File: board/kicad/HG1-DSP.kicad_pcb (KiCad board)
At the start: 12 copper layers, 150 x 150 mm, 29 parts, among them J2 Samtec LSHM-150 (mate ANT), J3 Samtec LSHM-150 (mate ANT), J4 Samtec LSHM-120 (mate ANT), J5 FFC to PWR/IO: GbE MDI, RS-48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, J6 Micro-Fit 4p: +12V_DSP in, U1 XCVE2302-1LSESFVA784 Versal A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, U10 nRF7002 Wi-Fi 6 2.4/5 GHz com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, U11 ISM330DHCX 6-axis IMU, U12 LIS2MDL magnetometer, U2 LPDDR4 32Gb x32 (MT53E1G32D2), U20 TPS546D24A 40 A PoL VCCINT 0.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, U21 TPS546D24A PoL VCC_AIE 0.8 V, U22 LT8640S 1V1/1V8/3V3 bucks, U3 LPDDR4 32Gb x32 (MT53E1G32D2), U4 eMMC 64 GB pSLC, U5 QSPI NOR 512 Mb (boot), U6 DP83867IR GbE PHY + IEEE1588 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, U7 STM32G474 housekeeping / powe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, U8 u-blox NEO-F10T GNSS timing (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, U9 nRF52840 BT5 LR Remote-ID rx

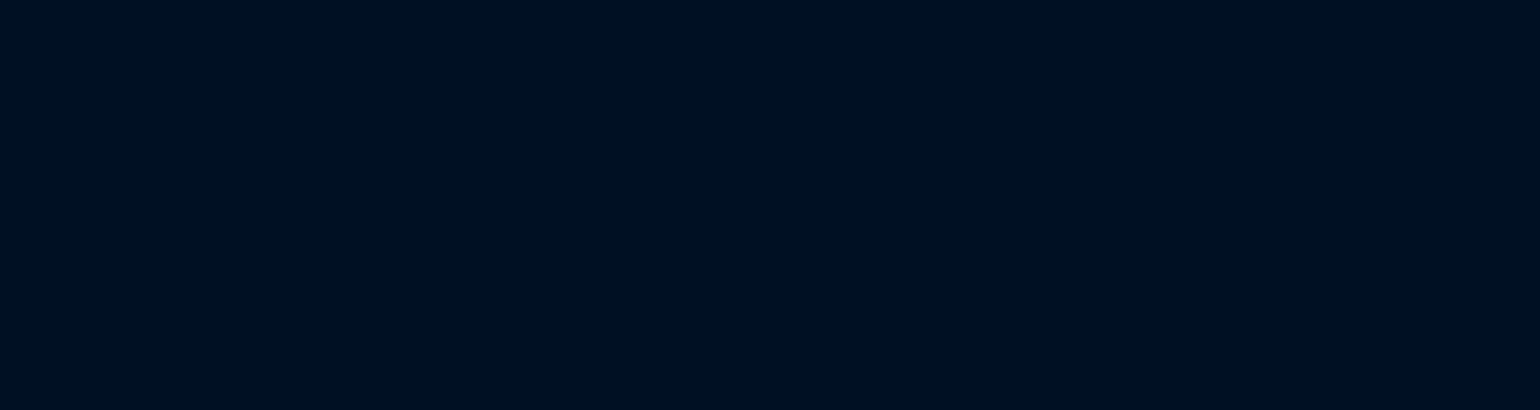
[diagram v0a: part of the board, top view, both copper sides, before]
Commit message: Schematics, full-wave EM element optimisation, physical stack-ups
Schematics
- KiCad schematics for HG1-ANT/DSP/PWR generated by board/schematic/
  (33-symbol HG1 library, pins taken from the routed layout): ERC 0/0,
  schematic<->PCB parity clean; scripted "Update PCB from Schematic"
  links footprints, nets and values and stages unplaced parts.
- STM32G474 pin map corrected to the real LQFP-64 pin-out.

Full-wave EM of the radiating element (antenna/em, docs/06)
- EMerge FEM models: isolated element and infinite-array unit cell with
  a scan-matched Floquet port; local PARDISO and Modal (CPU, cuDSS GPU).
- Found and fixed: low slot/superstrate resonance of the analytic cut,
  60 deg azimuth scan blindness (element via-fence cavity), far-field
  dB scaling and E/H cut labelling.
- Differential evolution on Modal (792 solves, worst of 0/45/60 deg):
  driven 3.21 mm, parasitic 4.48 mm, slot 3.02 mm + 2.14 mm arms,
  stub 1.50 mm, 1.016 mm parasitic spacer. Active |S11| < -10 dB over
  0.52-0.70 GHz around 16 GHz at every scan to 60 az / 40 el.

Board / mechanical
- New element copper and 1,051 blind L1-L5 element-fence vias on ANT.
- Full physical stack-ups (hg1_params.STACKS) written into each
  .kicad_pcb; ANT is 2.716 mm (old 2.1 mm could not hold 10 layers).
- Enclosure, mass (1,059 g), KiCad and Blender renders regenerated.
  DRC 0 errors on all boards, parity clean.

Co-Authored-By: Claude Opus 5.5 <noreply@anthropic.com>
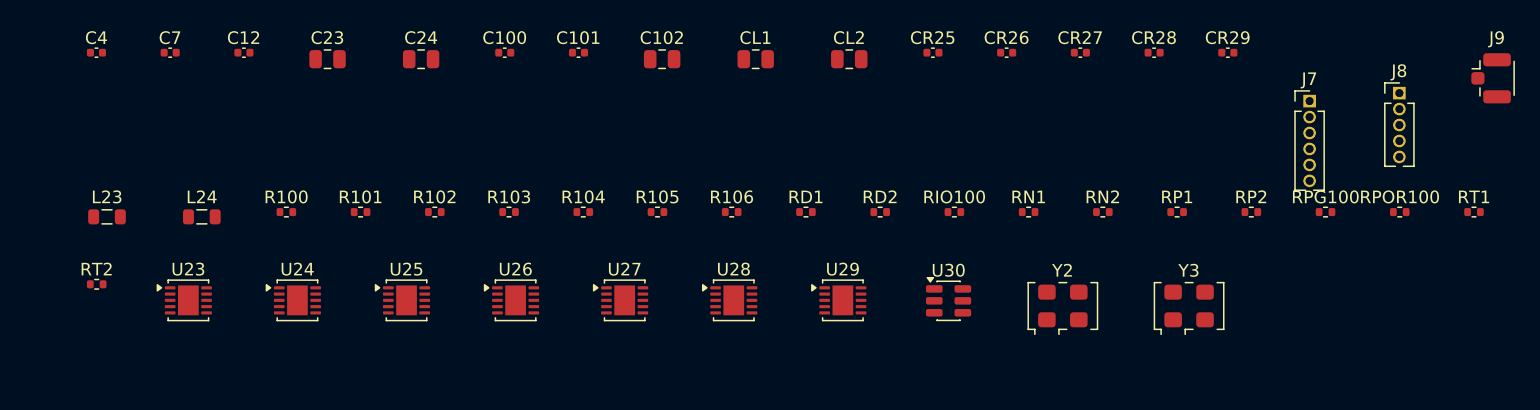
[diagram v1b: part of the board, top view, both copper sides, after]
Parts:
- added C100: 100n, Capacitor_SMD:C_0402_1005Metric, F.Cu at (275.4, 37.5)
- added C101: 1u, Capacitor_SMD:C_0402_1005Metric, F.Cu at (281.3, 37.5)
- added C102: 47u, Capacitor_SMD:C_0805_2012Metric, F.Cu at (288.0, 38.0)
- added C12: 220n, Capacitor_SMD:C_0402_1005Metric, F.Cu at (254.7, 37.5)
- added C23: 22u, Capacitor_SMD:C_0805_2012Metric, F.Cu at (261.3, 38.0)
- added C24: 22u, Capacitor_SMD:C_0805_2012Metric, F.Cu at (268.8, 38.0)
- added C4: 1u, Capacitor_SMD:C_0402_1005Metric, F.Cu at (242.9, 37.5)
- added C7: 100n, Capacitor_SMD:C_0402_1005Metric, F.Cu at (248.8, 37.5)
- added CL1: 470u polymer, Capacitor_SMD:C_0805_2012Metric, F.Cu at (295.4, 38.0)
- added CL2: 470u polymer, Capacitor_SMD:C_0805_2012Metric, F.Cu at (302.9, 38.0)
- added CR25: 1u, Capacitor_SMD:C_0402_1005Metric, F.Cu at (309.5, 37.5)
- added CR26: 1u, Capacitor_SMD:C_0402_1005Metric, F.Cu at (315.4, 37.5)
- added CR27: 1u, Capacitor_SMD:C_0402_1005Metric, F.Cu at (321.3, 37.5)
- added CR28: 1u, Capacitor_SMD:C_0402_1005Metric, F.Cu at (327.1, 37.5)
- added CR29: 1u, Capacitor_SMD:C_0402_1005Metric, F.Cu at (333.0, 37.5)
- added J7: JTAG, Connector_PinHeader_1.27mm:PinHeader_1x06_P1.27mm_Vertical, F.Cu at (339.5, 41.3)
- added J8: SWD (Tag-Connect TC2030), Connector_PinHeader_1.27mm:PinHeader_1x05_P1.27mm_Vertical, F.Cu at (346.7, 40.7)
- added J9: U.FL OTA-cal port, Connector_Coaxial:U.FL_Hirose_U.FL-R-SMT-1_Vertical, F.Cu at (354.4, 39.5)
- added L23: 2.2u, Inductor_SMD:L_0805_2012Metric, F.Cu at (243.8, 50.6)
- added L24: 2.2u, Inductor_SMD:L_0805_2012Metric, F.Cu at (251.3, 50.6)
- added R100: 1M, Resistor_SMD:R_0402_1005Metric, F.Cu at (258.1, 50.2)
- added R101: 316k, Resistor_SMD:R_0402_1005Metric, F.Cu at (264.0, 50.2)
- added R102: 18.2k, Resistor_SMD:R_0402_1005Metric, F.Cu at (269.9, 50.2)
- added R103: 100k, Resistor_SMD:R_0402_1005Metric, F.Cu at (275.8, 50.2)
- added R104: 49.9k, Resistor_SMD:R_0402_1005Metric, F.Cu at (281.7, 50.2)
- added R105: 100k, Resistor_SMD:R_0402_1005Metric, F.Cu at (287.6, 50.2)
- added R106: 49.9k, Resistor_SMD:R_0402_1005Metric, F.Cu at (293.5, 50.2)
- added RD1: 10k, Resistor_SMD:R_0402_1005Metric, F.Cu at (299.4, 50.2)
- added RD2: 10k, Resistor_SMD:R_0402_1005Metric, F.Cu at (305.3, 50.2)
- added RIO100: 0R (3.3 V to PWR/IO board), Resistor_SMD:R_0402_1005Metric, F.Cu at (311.2, 50.2)
- added RN1: 20k 0.1%, Resistor_SMD:R_0402_1005Metric, F.Cu at (317.2, 50.2)
- added RN2: 40.2k 0.1%, Resistor_SMD:R_0402_1005Metric, F.Cu at (323.1, 50.2)
- added RP1: 10k 0.1%, Resistor_SMD:R_0402_1005Metric, F.Cu at (329.0, 50.2)
- added RP2: 10k 0.1%, Resistor_SMD:R_0402_1005Metric, F.Cu at (334.9, 50.2)
- added RPG100: 10k, Resistor_SMD:R_0402_1005Metric, F.Cu at (340.8, 50.2)
- added RPOR100: 4.7k, Resistor_SMD:R_0402_1005Metric, F.Cu at (346.7, 50.2)
- added RT1: 10k B3435, Resistor_SMD:R_0402_1005Metric, F.Cu at (352.6, 50.2)
- added RT2: 10k B3435, Resistor_SMD:R_0402_1005Metric, F.Cu at (243.0, 55.9)
- added U23: TPS62913 1.8 V, Package_DFN_QFN:DFN-10-1EP_3x3mm_P0.5mm_EP1.65x2.38mm, F.Cu at (250.3, 57.2)
- added U24: TPS62913 1.1 V, Package_DFN_QFN:DFN-10-1EP_3x3mm_P0.5mm_EP1.65x2.38mm, F.Cu at (258.9, 57.2)
- added U25: ADP7159 1.5 V LDO, Package_DFN_QFN:DFN-10-1EP_3x3mm_P0.5mm_EP1.65x2.38mm, F.Cu at (267.6, 57.2)
- added U26: ADP7159 0.88 V LDO, Package_DFN_QFN:DFN-10-1EP_3x3mm_P0.5mm_EP1.65x2.38mm, F.Cu at (276.3, 57.2)
- added U27: ADP7159 1.2 V LDO, Package_DFN_QFN:DFN-10-1EP_3x3mm_P0.5mm_EP1.65x2.38mm, F.Cu at (285.0, 57.2)
- added U28: ADP7159 2.5 V LDO, Package_DFN_QFN:DFN-10-1EP_3x3mm_P0.5mm_EP1.65x2.38mm, F.Cu at (293.7, 57.2)
- added U29: ADP7159 1.0 V LDO, Package_DFN_QFN:DFN-10-1EP_3x3mm_P0.5mm_EP1.65x2.38mm, F.Cu at (302.4, 57.2)
- added U30: TPS3700 -5 V window, Package_TO_SOT_SMD:SOT-23-6, F.Cu at (310.8, 57.2)
- added Y2: 33.333 MHz XO (PS_REFCLK), Oscillator:Oscillator_SMD_EuroQuartz_XO53-4Pin_5.0x3.2mm, F.Cu at (319.9, 57.7)
- added Y3: 25 MHz XO, Oscillator:Oscillator_SMD_EuroQuartz_XO53-4Pin_5.0x3.2mm, F.Cu at (329.9, 57.7)
- H1, H2, H3, H4, H5, H6: footprint MountingHole_2.7mm_M2.5_Pad_Via -> MountingHole:MountingHole_2.7mm_M2.5_Pad_Via
- J2, J3: value Samtec LSHM-150 (mate ANT) -> LSHM-150 (mate ANT); footprint Samtec_LSHM-150-xx.x-x-DV-N_2x50_P0.50mm_Vertical -> Connector_Samtec:Samtec_LSHM-150-xx.x-x-DV-N_2x50_P0.50mm_Vertical
- J4: value Samtec LSHM-120 (mate ANT) -> LSHM-120 (mate ANT); footprint Samtec_LSHM-120-xx.x-x-DV-N_2x20_P0.50mm_Vertical -> Connector_Samtec:Samtec_LSHM-120-xx.x-x-DV-N_2x20_P0.50mm_Vertical
- J5: value FFC to PWR/IO: GbE MDI, RS-485, 1PPS, discretes -> FFC to PWR/IO; footprint Hirose_FH12-30S-0.5SH_1x30-1MP_P0.50mm_Horizontal -> Connector_FFC-FPC:Hirose_FH12-30S-0.5SH_1x30-1MP_P0.50mm_Horizontal
- J6: value Micro-Fit 4p: +12V_DSP in -> Micro-Fit +12V in; footprint Molex_Micro-Fit_3.0_43650-0400_1x04_P3.00mm_Horizontal -> Connector_Molex:Molex_Micro-Fit_3.0_43650-0400_1x04_P3.00mm_Horizontal
- L1, L2: value XAL6030 0.22 uH -> XAL6030 0.22u; footprint L_Coilcraft_XAL6030-XXX -> Inductor_SMD:L_Coilcraft_XAL6030-XXX
- L3: value XAL6030 1.0 uH -> XAL6030 1.0u; footprint L_Coilcraft_XAL6030-XXX -> Inductor_SMD:L_Coilcraft_XAL6030-XXX
- U1: value XCVE2302-1LSESFVA784 Versal AI Edge (AIE-ML 3D beamforming) -> XCVE2302-1LSESFVA784; footprint Microchip_FCVG784_BGA-784_23x23mm_Layout28x28_P0.8mm -> Package_BGA:Microchip_FCVG784_BGA-784_23x23mm_Layout28x28_P0.8mm
- U10: value nRF7002 Wi-Fi 6 2.4/5 GHz companion: Wi-Fi Beacon/NAN Remote-ID rx (fed from ANT RID patch) -> nRF7002; footprint QFN-40-1EP_6x6mm_P0.5mm_EP4.6x4.6mm -> Package_DFN_QFN:QFN-40-1EP_6x6mm_P0.5mm_EP4.6x4.6mm
- U11: value ISM330DHCX 6-axis IMU -> ISM330DHCX; footprint Bosch_LGA-14_3x2.5mm_P0.5mm -> Package_LGA:Bosch_LGA-14_3x2.5mm_P0.5mm
- U12: value LIS2MDL magnetometer -> LIS2MDL; footprint LGA-12_2x2mm_P0.5mm -> Package_LGA:LGA-12_2x2mm_P0.5mm
- U2, U3: value LPDDR4 32Gb x32 (MT53E1G32D2) -> MT53E1G32D2 LPDDR4; footprint BGA-200_10x14.5mm_Layout12x22_P0.8x0.65mm -> Package_BGA:BGA-200_10x14.5mm_Layout12x22_P0.8x0.65mm
- U20: value TPS546D24A 40 A PoL VCCINT 0.8 V -> TPS546D24A 0.8 V; footprint QFN-40-1EP_6x6mm_P0.5mm_EP4.6x4.6mm_ThermalVias -> Package_DFN_QFN:QFN-40-1EP_6x6mm_P0.5mm_EP4.6x4.6mm_ThermalVias
- U21: value TPS546D24A PoL VCC_AIE 0.8 V -> TPS546D24A 0.8 V; footprint QFN-40-1EP_6x6mm_P0.5mm_EP4.6x4.6mm_ThermalVias -> Package_DFN_QFN:QFN-40-1EP_6x6mm_P0.5mm_EP4.6x4.6mm_ThermalVias
- U22: value LT8640S 1V1/1V8/3V3 bucks -> LT8640S 3.3 V; footprint QFN-24-1EP_4x4mm_P0.5mm_EP2.6x2.6mm -> Package_DFN_QFN:QFN-24-1EP_4x4mm_P0.5mm_EP2.6x2.6mm
- U4: footprint LFBGA-153_11.5x13mm_Layout14x14_P0.5mm -> Package_BGA:LFBGA-153_11.5x13mm_Layout14x14_P0.5mm
- U5: value QSPI NOR 512 Mb (boot) -> MT25QU512 QSPI; footprint WSON-8-1EP_8x6mm_P1.27mm_EP3.4x4.3mm -> Package_SON:WSON-8-1EP_8x6mm_P1.27mm_EP3.4x4.3mm
- U6: value DP83867IR GbE PHY + IEEE1588 SFD -> DP83867IRRGZ; footprint QFN-48-1EP_7x7mm_P0.5mm_EP5.6x5.6mm -> Package_DFN_QFN:QFN-48-1EP_7x7mm_P0.5mm_EP5.6x5.6mm
- U7: value STM32G474 housekeeping / power-seq / BIT -> STM32G474RET6; footprint LQFP-64_10x10mm_P0.5mm -> Package_QFP:LQFP-64_10x10mm_P0.5mm
- U8: value u-blox NEO-F10T GNSS timing (L1/L5) -> NEO-F10T (NEO footprint); footprint ublox_NEO -> RF_GPS:ublox_NEO
- U9: value nRF52840 BT5 LR Remote-ID rx -> MDBT50Q nRF52840; footprint Raytac_MDBT50Q -> RF_Module:Raytac_MDBT50Q
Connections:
- J2 pad 1: (no net) -> GND
- J2 pad 10: (no net) -> GND
- J2 pad 100: (no net) -> JESD1_L0
- J2 pad 11: (no net) -> GND
- J2 pad 12: (no net) -> GND
- J2 pad 13: (no net) -> GND
- J2 pad 14: (no net) -> GND
- J2 pad 15: (no net) -> GND
- J2 pad 16: (no net) -> GND
- J2 pad 17: (no net) -> GND
- J2 pad 18: (no net) -> GND
- J2 pad 19: (no net) -> GND
- J2 pad 2: (no net) -> JESD3_L3
- J2 pad 20: (no net) -> JESD2_L3
- J2 pad 21: (no net) -> GND
- J2 pad 22: (no net) -> GND
- J2 pad 23: (no net) -> GND
- J2 pad 24: (no net) -> JESD2_L2
- J2 pad 25: (no net) -> GND
- J2 pad 26: (no net) -> JESD2_L1
- J2 pad 27: (no net) -> GND
- J2 pad 28: (no net) -> GND
- J2 pad 29: (no net) -> GND
- J2 pad 3: (no net) -> CAL_PROBE
- J2 pad 30: (no net) -> JESD2_L0
- J2 pad 31: (no net) -> GND
- J2 pad 32: (no net) -> GND
- J2 pad 33: (no net) -> GND
- J2 pad 34: (no net) -> GND
- J2 pad 35: (no net) -> GND
- J2 pad 36: (no net) -> GND
- J2 pad 37: (no net) -> GND
- J2 pad 38: (no net) -> GND
- J2 pad 39: (no net) -> GND
- J2 pad 4: (no net) -> JESD3_L2
- J2 pad 40: (no net) -> GND
- J2 pad 41: (no net) -> GND
- J2 pad 42: (no net) -> GND
- J2 pad 43: (no net) -> GND
- J2 pad 44: (no net) -> GND
- J2 pad 45: (no net) -> GND
- J2 pad 46: (no net) -> GND
- J2 pad 47: (no net) -> GND
- J2 pad 48: (no net) -> GND
- J2 pad 49: (no net) -> GND
- J2 pad 5: (no net) -> CAL_PROBE
- J2 pad 50: (no net) -> GND
- J2 pad 51: (no net) -> GND
- J2 pad 52: (no net) -> GND
- J2 pad 53: (no net) -> GND
- J2 pad 54: (no net) -> GND
- J2 pad 55: (no net) -> GND
- J2 pad 56: (no net) -> GND
- J2 pad 57: (no net) -> GND
- J2 pad 58: (no net) -> GND
- J2 pad 59: (no net) -> GND
- J2 pad 6: (no net) -> JESD3_L1
- J2 pad 60: (no net) -> GND
- J2 pad 61: (no net) -> GND
- J2 pad 62: (no net) -> GND
- J2 pad 63: (no net) -> GND
- J2 pad 64: (no net) -> GND
- J2 pad 65: (no net) -> GND
- J2 pad 66: (no net) -> GND
- J2 pad 67: (no net) -> GND
- J2 pad 68: (no net) -> GND
- J2 pad 69: (no net) -> GND
- J2 pad 7: (no net) -> CAL_PROBE
- J2 pad 70: (no net) -> GND
- J2 pad 71: (no net) -> GND
- J2 pad 72: (no net) -> GND
- J2 pad 73: (no net) -> GND
- J2 pad 74: (no net) -> GND
- J2 pad 75: (no net) -> GND
- J2 pad 76: (no net) -> GND
- J2 pad 77: (no net) -> GND
- J2 pad 78: (no net) -> GND
- J2 pad 79: (no net) -> GND
- J2 pad 8: (no net) -> JESD3_L0
- J2 pad 80: (no net) -> GND
- J2 pad 81: (no net) -> GND
- J2 pad 82: (no net) -> GND
- J2 pad 83: (no net) -> GND
- J2 pad 84: (no net) -> GND
- J2 pad 85: (no net) -> GND
- J2 pad 86: (no net) -> GND
- J2 pad 87: (no net) -> GND
- J2 pad 88: (no net) -> GND
- J2 pad 89: (no net) -> GND
- J2 pad 9: (no net) -> CAL_PROBE
- J2 pad 90: (no net) -> GND
- J2 pad 91: (no net) -> GND
- J2 pad 92: (no net) -> JESD1_L3
- J2 pad 93: (no net) -> GND
- J2 pad 94: (no net) -> GND
- J2 pad 95: (no net) -> GND
- J2 pad 96: (no net) -> JESD1_L2
- J2 pad 97: (no net) -> GND
- J2 pad 98: (no net) -> JESD1_L1
- J2 pad 99: (no net) -> GND
- J3 pad 1: (no net) -> GND
- J3 pad 10: (no net) -> JESD6_L1
- J3 pad 100: (no net) -> JESD4_L0
- J3 pad 11: (no net) -> ID_PA2
- J3 pad 12: (no net) -> GND
- J3 pad 13: (no net) -> GND
- J3 pad 14: (no net) -> JESD6_L0
- J3 pad 15: (no net) -> ID_PA3
- J3 pad 16: (no net) -> GND
- J3 pad 17: (no net) -> ID_PA4
- J3 pad 18: (no net) -> GND
- J3 pad 19: (no net) -> ID_PA5
- J3 pad 2: (no net) -> GND
- J3 pad 20: (no net) -> GND
- J3 pad 21: (no net) -> ID_PA6
- J3 pad 22: (no net) -> GND
- J3 pad 23: (no net) -> ID_PA1
- J3 pad 24: (no net) -> GND
- J3 pad 25: (no net) -> ID_PA2
- J3 pad 26: (no net) -> GND
- J3 pad 27: (no net) -> ID_PA3
- J3 pad 28: (no net) -> GND
- J3 pad 29: (no net) -> ID_PA4
- J3 pad 3: (no net) -> GND
- J3 pad 30: (no net) -> GND
- J3 pad 31: (no net) -> ID_PA5
- J3 pad 32: (no net) -> GND
- J3 pad 33: (no net) -> ID_PA6
- J3 pad 34: (no net) -> GND
- J3 pad 35: (no net) -> ID_PA1
- J3 pad 36: (no net) -> GND
- J3 pad 37: (no net) -> ID_PA2
- J3 pad 38: (no net) -> GND
- J3 pad 39: (no net) -> ID_PA3
- J3 pad 4: (no net) -> JESD6_L3
- J3 pad 40: (no net) -> GND
- J3 pad 41: (no net) -> ID_PA4
- J3 pad 42: (no net) -> GND
- J3 pad 43: (no net) -> ID_PA5
- J3 pad 44: (no net) -> GND
- J3 pad 45: (no net) -> ID_PA6
- J3 pad 46: (no net) -> GND
- J3 pad 47: (no net) -> ID_PA1
- J3 pad 48: (no net) -> GND
- J3 pad 49: (no net) -> ID_PA2
- J3 pad 5: (no net) -> ID_PA1
- J3 pad 50: (no net) -> GND
- J3 pad 51: (no net) -> ID_PA3
- J3 pad 52: (no net) -> GND
- J3 pad 53: (no net) -> ID_PA4
- J3 pad 54: (no net) -> GND
- J3 pad 55: (no net) -> ID_PA5
- J3 pad 56: (no net) -> GND
- J3 pad 57: (no net) -> ID_PA6
- J3 pad 58: (no net) -> GND
- J3 pad 59: (no net) -> GND
- J3 pad 6: (no net) -> GND
- J3 pad 60: (no net) -> GND
- J3 pad 61: (no net) -> GND
- J3 pad 62: (no net) -> GND
- J3 pad 63: (no net) -> GND
- J3 pad 64: (no net) -> GND
- J3 pad 65: (no net) -> GND
- J3 pad 66: (no net) -> GND
- J3 pad 67: (no net) -> GND
- J3 pad 68: (no net) -> GND
- J3 pad 69: (no net) -> GND
- J3 pad 7: (no net) -> GND
- J3 pad 70: (no net) -> GND
- J3 pad 71: (no net) -> GND
- J3 pad 72: (no net) -> GND
- J3 pad 73: (no net) -> GND
- J3 pad 74: (no net) -> GND
- J3 pad 75: (no net) -> GND
- J3 pad 76: (no net) -> JESD5_L3
- J3 pad 77: (no net) -> GND
- J3 pad 78: (no net) -> GND
- J3 pad 79: (no net) -> GND
- J3 pad 8: (no net) -> JESD6_L2
- J3 pad 80: (no net) -> JESD5_L2
- J3 pad 81: (no net) -> GND
- J3 pad 82: (no net) -> JESD5_L1
- J3 pad 83: (no net) -> GND
- J3 pad 84: (no net) -> GND
- J3 pad 85: (no net) -> GND
- J3 pad 86: (no net) -> JESD5_L0
- J3 pad 87: (no net) -> GND
- J3 pad 88: (no net) -> GND
- J3 pad 89: (no net) -> GND
- J3 pad 9: (no net) -> GND
- J3 pad 90: (no net) -> GND
- J3 pad 91: (no net) -> GND
- J3 pad 92: (no net) -> GND
- J3 pad 93: (no net) -> GND
- J3 pad 94: (no net) -> JESD4_L3
- J3 pad 95: (no net) -> GND
- J3 pad 96: (no net) -> JESD4_L2
- J3 pad 97: (no net) -> GND
- J3 pad 98: (no net) -> JESD4_L1
- J3 pad 99: (no net) -> GND
- J4 pad 1: (no net) -> SPI_SCLK
- J4 pad 10: (no net) -> CS_ADC0
- J4 pad 11: (no net) -> CS_ADC1
- J4 pad 12: (no net) -> CS_ADC2
- J4 pad 13: (no net) -> CS_ADC3
- J4 pad 14: (no net) -> CS_ADC4
- J4 pad 15: (no net) -> CS_ADC5
- J4 pad 16: (no net) -> CS_PLL_TX
- J4 pad 17: (no net) -> CS_PLL_LO
- J4 pad 18: (no net) -> CS_CLK
- J4 pad 19: (no net) -> CHIRP_TRIG
- J4 pad 2: (no net) -> GND
- J4 pad 20: (no net) -> JESD_SYNC
- J4 pad 21: (no net) -> PLL_LD_TX
- J4 pad 22: (no net) -> PLL_LD_LO
- J4 pad 23: (no net) -> FPGA_REFCLK
- J4 pad 24: (no net) -> FPGA_SYSREF
- J4 pad 25: (no net) -> MCU_SPI_SCK
- J4 pad 26: (no net) -> MCU_SPI_MOSI
- J4 pad 27: (no net) -> MCU_SPI_MISO
- J4 pad 28: (no net) -> CS_BF0
- J4 pad 29: (no net) -> CS_BF1
- J4 pad 3: (no net) -> SPI_MOSI
- J4 pad 30: (no net) -> TX_MUTE_N
- J4 pad 31: (no net) -> TX_LOAD
- J4 pad 32: (no net) -> EN_DRAIN_SW
- J4 pad 33: (no net) -> I2C3_SCL
- J4 pad 34: (no net) -> I2C3_SDA
- J4 pad 35: (no net) -> GNSS_RF
- J4 pad 36: (no net) -> RID_RF
- J4 pad 37: (no net) -> -5V_BIAS
- J4 pad 38: (no net) -> RF_RESET_N
- J4 pad 39: (no net) -> GND
- J4 pad 4: (no net) -> CS_RFIC0
- J4 pad 40: (no net) -> GND
- J4 pad 5: (no net) -> CS_RFIC1
- J4 pad 6: (no net) -> CS_RFIC2
- J4 pad 7: (no net) -> CS_RFIC3
- J4 pad 8: (no net) -> CS_RFIC4
- J4 pad 9: (no net) -> CS_RFIC5
- J5 pad 1: (no net) -> PHY_MD1
- J5 pad 10: (no net) -> PHY_MD7
- J5 pad 11: (no net) -> PHY_MD8
- J5 pad 12: (no net) -> GND
- J5 pad 13: (no net) -> RS485_TX
- J5 pad 14: (no net) -> RS485_RX
- J5 pad 15: (no net) -> RS485_DE
- J5 pad 16: (no net) -> PPS_EXT
- J5 pad 17: (no net) -> DISC_IN
- J5 pad 18: (no net) -> EN_28V
- J5 pad 19: (no net) -> EN_NEG5
- J5 pad 2: (no net) -> PHY_MD2
- J5 pad 20: (no net) -> EN_RF_5V
- J5 pad 21: (no net) -> EN_HEATER
- J5 pad 22: (no net) -> VIN_SENSE
- J5 pad 23: (no net) -> V28_SENSE
- J5 pad 24: (no net) -> V5_SENSE
- J5 pad 25: (no net) -> -5V_BIAS
- J5 pad 26: (no net) -> -5V_BIAS
- J5 pad 27: (no net) -> +3V3_IO
- J5 pad 28: (no net) -> GND
- J5 pad 29: (no net) -> GND
- J5 pad 3: (no net) -> GND
- J5 pad 30: (no net) -> GND
- J5 pad 4: (no net) -> PHY_MD3
- J5 pad 5: (no net) -> PHY_MD4
- J5 pad 6: (no net) -> GND
- J5 pad 7: (no net) -> PHY_MD5
- J5 pad 8: (no net) -> PHY_MD6
- J5 pad 9: (no net) -> GND
- J6 pad 1: (no net) -> +12V
- J6 pad 2: (no net) -> +12V
- J6 pad 3: (no net) -> GND
- J6 pad 4: (no net) -> GND
- L1 pad 1: (no net) -> SW_VCCINT
- L1 pad 2: (no net) -> VCCINT_0V8
- L2 pad 1: (no net) -> SW_AIE
- L2 pad 2: (no net) -> VCC_AIE_0V8
- L3 pad 1: (no net) -> SW_3V3
- L3 pad 2: (no net) -> +3V3
- U1 pad A1: (no net) -> JESD1_L0
- U1 pad A10: (no net) -> JESD3_L1
- U1 pad A11: (no net) -> JESD3_L2
- U1 pad A12: (no net) -> JESD3_L3
- U1 pad A13: (no net) -> JESD4_L0
- U1 pad A14: (no net) -> JESD4_L1
- U1 pad A15: (no net) -> JESD4_L2
- U1 pad A16: (no net) -> JESD4_L3
- U1 pad A17: (no net) -> JESD5_L0
- U1 pad A18: (no net) -> JESD5_L1
- U1 pad A19: (no net) -> JESD5_L2
- U1 pad A2: (no net) -> JESD1_L1
- U1 pad A20: (no net) -> JESD5_L3
- U1 pad A21: (no net) -> JESD6_L0
- U1 pad A22: (no net) -> JESD6_L1
- U1 pad A23: (no net) -> JESD6_L2
- U1 pad A24: (no net) -> JESD6_L3
- U1 pad A25: (no net) -> FPGA_REFCLK
- U1 pad A26: (no net) -> FPGA_SYSREF
- U1 pad A27: (no net) -> JESD_SYNC
- U1 pad A28: (no net) -> SPI_SCLK
- U1 pad A3: (no net) -> JESD1_L2
- U1 pad A4: (no net) -> JESD1_L3
- U1 pad A5: (no net) -> JESD2_L0
- U1 pad A6: (no net) -> JESD2_L1
- U1 pad A7: (no net) -> JESD2_L2
- U1 pad A8: (no net) -> JESD2_L3
- U1 pad A9: (no net) -> JESD3_L0
- U1 pad AA1: (no net) -> SPI_MOSI
- U1 pad AA10: (no net) -> CS_ADC1
- U1 pad AA11: (no net) -> CS_ADC2
- U1 pad AA12: (no net) -> CS_ADC3
- U1 pad AA13: (no net) -> CS_ADC4
- U1 pad AA14: (no net) -> CS_ADC5
- U1 pad AA15: (no net) -> CS_PLL_TX
- U1 pad AA16: (no net) -> CS_PLL_LO
- U1 pad AA17: (no net) -> CS_CLK
- U1 pad AA18: (no net) -> CHIRP_TRIG
- U1 pad AA19: (no net) -> TX_LOAD
- U1 pad AA2: (no net) -> unconnected-(U1-SPI_MISO-PadAA2)
- U1 pad AA20: (no net) -> PLL_LD_TX
- U1 pad AA21: (no net) -> PLL_LD_LO
- U1 pad AA22: (no net) -> DDRA_CA0
- U1 pad AA23: (no net) -> DDRA_CA1
- U1 pad AA24: (no net) -> DDRA_CA2
- U1 pad AA25: (no net) -> DDRA_CA3
- U1 pad AA26: (no net) -> DDRA_CA4
- U1 pad AA27: (no net) -> DDRA_CA5
- U1 pad AA28: (no net) -> DDRA_CS
- U1 pad AA3: (no net) -> CS_RFIC0
- U1 pad AA4: (no net) -> CS_RFIC1
- U1 pad AA5: (no net) -> CS_RFIC2
- U1 pad AA6: (no net) -> CS_RFIC3
- U1 pad AA7: (no net) -> CS_RFIC4
- U1 pad AA8: (no net) -> CS_RFIC5
- U1 pad AA9: (no net) -> CS_ADC0
- U1 pad AB1: (no net) -> DDRA_CKE
- U1 pad AB10: (no net) -> DDRA_DQ5
- U1 pad AB11: (no net) -> DDRA_DQ6
- U1 pad AB12: (no net) -> DDRA_DQ7
- U1 pad AB13: (no net) -> DDRA_DQ8
- U1 pad AB14: (no net) -> DDRA_DQ9
- U1 pad AB15: (no net) -> DDRA_DQ10
- U1 pad AB16: (no net) -> DDRA_DQ11
- U1 pad AB17: (no net) -> DDRA_DQ12
- U1 pad AB18: (no net) -> DDRA_DQ13
- U1 pad AB19: (no net) -> DDRA_DQ14
- U1 pad AB2: (no net) -> DDRA_CK_T
- U1 pad AB20: (no net) -> DDRA_DQ15
- U1 pad AB21: (no net) -> DDRA_DQ16
- U1 pad AB22: (no net) -> DDRA_DQ17
- U1 pad AB23: (no net) -> DDRA_DQ18
- U1 pad AB24: (no net) -> DDRA_DQ19
- U1 pad AB25: (no net) -> DDRA_DQ20
- U1 pad AB26: (no net) -> DDRA_DQ21
- U1 pad AB27: (no net) -> DDRA_DQ22
- U1 pad AB28: (no net) -> DDRA_DQ23
- U1 pad AB3: (no net) -> DDRA_CK_C
- U1 pad AB4: (no net) -> DDRA_RESET_N
- U1 pad AB5: (no net) -> DDRA_DQ0
- U1 pad AB6: (no net) -> DDRA_DQ1
- U1 pad AB7: (no net) -> DDRA_DQ2
- U1 pad AB8: (no net) -> DDRA_DQ3
- U1 pad AB9: (no net) -> DDRA_DQ4
- U1 pad AC1: (no net) -> DDRA_DQ24
- U1 pad AC10: (no net) -> DDRA_DQS_T1
- U1 pad AC11: (no net) -> DDRA_DQS_T2
- U1 pad AC12: (no net) -> DDRA_DQS_T3
- U1 pad AC13: (no net) -> DDRA_DQS_C0
- U1 pad AC14: (no net) -> DDRA_DQS_C1
- U1 pad AC15: (no net) -> DDRA_DQS_C2
- U1 pad AC16: (no net) -> DDRA_DQS_C3
- U1 pad AC17: (no net) -> DDRA_DMI0
- U1 pad AC18: (no net) -> DDRA_DMI1
- U1 pad AC19: (no net) -> DDRA_DMI2
- U1 pad AC2: (no net) -> DDRA_DQ25
- U1 pad AC20: (no net) -> DDRA_DMI3
- U1 pad AC21: (no net) -> DDRB_CA0
- U1 pad AC22: (no net) -> DDRB_CA1
- U1 pad AC23: (no net) -> DDRB_CA2
- U1 pad AC24: (no net) -> DDRB_CA3
- U1 pad AC25: (no net) -> DDRB_CA4
- U1 pad AC26: (no net) -> DDRB_CA5
- U1 pad AC27: (no net) -> DDRB_CS
- U1 pad AC28: (no net) -> DDRB_CKE
- U1 pad AC3: (no net) -> DDRA_DQ26
- U1 pad AC4: (no net) -> DDRA_DQ27
- U1 pad AC5: (no net) -> DDRA_DQ28
- U1 pad AC6: (no net) -> DDRA_DQ29
- U1 pad AC7: (no net) -> DDRA_DQ30
- U1 pad AC8: (no net) -> DDRA_DQ31
- U1 pad AC9: (no net) -> DDRA_DQS_T0
- U1 pad AD1: (no net) -> DDRB_CK_T
- U1 pad AD10: (no net) -> DDRB_DQ6
- U1 pad AD11: (no net) -> DDRB_DQ7
- U1 pad AD12: (no net) -> DDRB_DQ8
- U1 pad AD13: (no net) -> DDRB_DQ9
- U1 pad AD14: (no net) -> DDRB_DQ10
- U1 pad AD15: (no net) -> DDRB_DQ11
- U1 pad AD16: (no net) -> DDRB_DQ12
- U1 pad AD17: (no net) -> DDRB_DQ13
- U1 pad AD18: (no net) -> DDRB_DQ14
- U1 pad AD19: (no net) -> DDRB_DQ15
- U1 pad AD2: (no net) -> DDRB_CK_C
- U1 pad AD20: (no net) -> DDRB_DQ16
- U1 pad AD21: (no net) -> DDRB_DQ17
- U1 pad AD22: (no net) -> DDRB_DQ18
- U1 pad AD23: (no net) -> DDRB_DQ19
- U1 pad AD24: (no net) -> DDRB_DQ20
- U1 pad AD25: (no net) -> DDRB_DQ21
- U1 pad AD26: (no net) -> DDRB_DQ22
- U1 pad AD27: (no net) -> DDRB_DQ23
- U1 pad AD28: (no net) -> DDRB_DQ24
- U1 pad AD3: (no net) -> DDRB_RESET_N
- U1 pad AD4: (no net) -> DDRB_DQ0
- U1 pad AD5: (no net) -> DDRB_DQ1
- U1 pad AD6: (no net) -> DDRB_DQ2
- U1 pad AD7: (no net) -> DDRB_DQ3
- U1 pad AD8: (no net) -> DDRB_DQ4
- U1 pad AD9: (no net) -> DDRB_DQ5
- U1 pad AE1: (no net) -> DDRB_DQ25
- U1 pad AE10: (no net) -> DDRB_DQS_T2
- U1 pad AE11: (no net) -> DDRB_DQS_T3
- U1 pad AE12: (no net) -> DDRB_DQS_C0
- U1 pad AE13: (no net) -> DDRB_DQS_C1
- U1 pad AE14: (no net) -> DDRB_DQS_C2
- U1 pad AE15: (no net) -> DDRB_DQS_C3
- U1 pad AE16: (no net) -> DDRB_DMI0
- U1 pad AE17: (no net) -> DDRB_DMI1
- U1 pad AE18: (no net) -> DDRB_DMI2
- U1 pad AE19: (no net) -> DDRB_DMI3
- U1 pad AE2: (no net) -> DDRB_DQ26
- U1 pad AE20: (no net) -> EMMC_CLK
- U1 pad AE21: (no net) -> EMMC_CMD
- U1 pad AE22: (no net) -> EMMC_D0
- U1 pad AE23: (no net) -> EMMC_D1
- U1 pad AE24: (no net) -> EMMC_D2
- U1 pad AE25: (no net) -> EMMC_D3
- U1 pad AE26: (no net) -> EMMC_D4
- U1 pad AE27: (no net) -> EMMC_D5
- U1 pad AE28: (no net) -> EMMC_D6
- U1 pad AE3: (no net) -> DDRB_DQ27
- U1 pad AE4: (no net) -> DDRB_DQ28
- U1 pad AE5: (no net) -> DDRB_DQ29
- U1 pad AE6: (no net) -> DDRB_DQ30
- U1 pad AE7: (no net) -> DDRB_DQ31
- U1 pad AE8: (no net) -> DDRB_DQS_T0
- U1 pad AE9: (no net) -> DDRB_DQS_T1
- U1 pad AF1: (no net) -> EMMC_D7
- U1 pad AF10: (no net) -> RGMII_TX_CTL
- U1 pad AF11: (no net) -> RGMII_TXD0
- U1 pad AF12: (no net) -> RGMII_TXD1
- U1 pad AF13: (no net) -> RGMII_TXD2
- U1 pad AF14: (no net) -> RGMII_TXD3
- U1 pad AF15: (no net) -> MDC
- U1 pad AF16: (no net) -> PHY_RST_N
- U1 pad AF17: (no net) -> RGMII_RXC
- U1 pad AF18: (no net) -> RGMII_RX_CTL
- U1 pad AF19: (no net) -> RGMII_RXD0
- U1 pad AF2: (no net) -> EMMC_RST_N
- U1 pad AF20: (no net) -> RGMII_RXD1
- U1 pad AF21: (no net) -> RGMII_RXD2
- U1 pad AF22: (no net) -> RGMII_RXD3
- U1 pad AF23: (no net) -> PHY_INT_N
- U1 pad AF24: (no net) -> MDIO
- U1 pad AF25: (no net) -> UART_V2M
- U1 pad AF26: (no net) -> UART_M2V
- U1 pad AF27: (no net) -> I2C3_SCL
- U1 pad AF28: (no net) -> I2C3_SDA
- U1 pad AF3: (no net) -> QSPI_CLK
- U1 pad AF4: (no net) -> QSPI_CS_N
- U1 pad AF5: (no net) -> QSPI_DQ0
- U1 pad AF6: (no net) -> QSPI_DQ1
- U1 pad AF7: (no net) -> QSPI_DQ2
- U1 pad AF8: (no net) -> QSPI_DQ3
- U1 pad AF9: (no net) -> RGMII_TXC
- U1 pad AG1: (no net) -> GNSS_RX
- U1 pad AG10: (no net) -> BLE_TX
- U1 pad AG11: (no net) -> BLE_RX
- U1 pad AG12: (no net) -> WIFI_SCK
- U1 pad AG13: (no net) -> WIFI_MOSI
- U1 pad AG14: (no net) -> WIFI_MISO
- U1 pad AG15: (no net) -> WIFI_CS
- U1 pad AG16: (no net) -> WIFI_IRQ
- U1 pad AG17: (no net) -> WIFI_EN
- U1 pad AG18: (no net) -> RS485_TX
- U1 pad AG19: (no net) -> RS485_RX
- U1 pad AG2: (no net) -> GNSS_TX
- U1 pad AG20: (no net) -> RS485_DE
- U1 pad AG21: (no net) -> PPS_EXT
- U1 pad AG22: (no net) -> DISC_IN
- U1 pad AG23: (no net) -> RF_RESET_N
- U1 pad AG24: (no net) -> JTAG_TCK
- U1 pad AG25: (no net) -> JTAG_TMS
- U1 pad AG26: (no net) -> JTAG_TDI
- U1 pad AG27: (no net) -> JTAG_TDO
- U1 pad AG28: (no net) -> POR_B
- U1 pad AG3: (no net) -> PPS
- U1 pad AG4: (no net) -> IMU_SCLK
- U1 pad AG5: (no net) -> IMU_MOSI
- U1 pad AG6: (no net) -> IMU_MISO
- U1 pad AG7: (no net) -> IMU_CS
- U1 pad AG8: (no net) -> MAG_CS
- U1 pad AG9: (no net) -> IMU_INT
- U1 pad AH1: (no net) -> PS_REFCLK
- U1 pad AH10: (no net) -> GND
- U1 pad AH2: (no net) -> VCCINT_0V8
- U1 pad AH3: (no net) -> VCC_AIE_0V8
- U1 pad AH4: (no net) -> +1V5_AUX
- U1 pad AH5: (no net) -> +1V1_DDR
- U1 pad AH6: (no net) -> +1V8
- U1 pad AH7: (no net) -> +3V3
- U1 pad AH8: (no net) -> +0V88_GT
- U1 pad AH9: (no net) -> +1V2_GT
- U10 pad 1: (no net) -> WIFI_SCK
- U10 pad 10: (no net) -> +3V3
- U10 pad 11: (no net) -> +3V3
- U10 pad 12: (no net) -> +1V8
- U10 pad 19: (no net) -> GND
- U10 pad 2: (no net) -> WIFI_MOSI
- U10 pad 20: (no net) -> RID_RF
- U10 pad 21: (no net) -> GND
- U10 pad 3: (no net) -> WIFI_MISO
- U10 pad 4: (no net) -> WIFI_CS
- U10 pad 41: (no net) -> GND
- U10 pad 5: (no net) -> WIFI_IRQ
- U10 pad 6: (no net) -> WIFI_EN
- U10 pad 7: (no net) -> WIFI_EN
- U11 pad 1: (no net) -> IMU_MISO
- U11 pad 10: (no net) -> unconnected-(U11-OCS_AUX-Pad10)
- U11 pad 11: (no net) -> unconnected-(U11-SDO_AUX-Pad11)
- U11 pad 12: (no net) -> IMU_CS
- U11 pad 13: (no net) -> IMU_SCLK
- U11 pad 14: (no net) -> IMU_MOSI
- U11 pad 2: (no net) -> unconnected-(U11-SDx-Pad2)
- U11 pad 3: (no net) -> unconnected-(U11-SCx-Pad3)
- U11 pad 4: (no net) -> IMU_INT
- U11 pad 5: (no net) -> +1V8
- U11 pad 6: (no net) -> GND
- U11 pad 7: (no net) -> GND
- U11 pad 8: (no net) -> +1V8
- U11 pad 9: (no net) -> unconnected-(U11-INT2-Pad9)
- U12 pad 1: (no net) -> IMU_SCLK
- U12 pad 10: (no net) -> +1V8
- U12 pad 11: (no net) -> unconnected-(U12-NC-Pad11)
- U12 pad 12: (no net) -> unconnected-(U12-NC-Pad12)
- U12 pad 2: (no net) -> unconnected-(U12-NC-Pad2)
- U12 pad 3: (no net) -> MAG_CS
- U12 pad 4: (no net) -> IMU_MOSI
- U12 pad 5: (no net) -> MAG_C1
- U12 pad 6: (no net) -> GND
- U12 pad 7: (no net) -> unconnected-(U12-DRDY-Pad7)
- U12 pad 8: (no net) -> GND
- U12 pad 9: (no net) -> +1V8
- U2 pad A1: (no net) -> DDRA_CA0
- U2 pad A10: (no net) -> DDRA_CKE
- U2 pad A11: (no net) -> DDRA_CK_T
- U2 pad A12: (no net) -> DDRA_CK_C
- U2 pad A2: (no net) -> DDRA_CA1
- U2 pad A3: (no net) -> DDRA_CA2
- U2 pad A4: (no net) -> DDRA_CA3
- U2 pad A5: (no net) -> DDRA_CA4
- U2 pad A8: (no net) -> DDRA_CA5
- U2 pad A9: (no net) -> DDRA_CS
- U2 pad AA1: (no net) -> DDRA_RESET_N
- U2 pad AA10: (no net) -> DDRA_DQ6
- U2 pad AA11: (no net) -> DDRA_DQ7
- U2 pad AA12: (no net) -> DDRA_DQ8
- U2 pad AA2: (no net) -> DDRA_DQ0
- U2 pad AA3: (no net) -> DDRA_DQ1
- U2 pad AA4: (no net) -> DDRA_DQ2
- U2 pad AA5: (no net) -> DDRA_DQ3
- U2 pad AA8: (no net) -> DDRA_DQ4
- U2 pad AA9: (no net) -> DDRA_DQ5
- U2 pad AB1: (no net) -> DDRA_DQ9
- U2 pad AB10: (no net) -> DDRA_DQ16
- U2 pad AB11: (no net) -> DDRA_DQ17
- U2 pad AB12: (no net) -> DDRA_DQ18
- U2 pad AB2: (no net) -> DDRA_DQ10
- U2 pad AB3: (no net) -> DDRA_DQ11
- U2 pad AB4: (no net) -> DDRA_DQ12
- U2 pad AB5: (no net) -> DDRA_DQ13
- U2 pad AB8: (no net) -> DDRA_DQ14
- U2 pad AB9: (no net) -> DDRA_DQ15
- U2 pad B1: (no net) -> DDRA_DQ19
- U2 pad B10: (no net) -> DDRA_DQ26
- U2 pad B11: (no net) -> DDRA_DQ27
- U2 pad B12: (no net) -> DDRA_DQ28
- U2 pad B2: (no net) -> DDRA_DQ20
- U2 pad B3: (no net) -> DDRA_DQ21
- U2 pad B4: (no net) -> DDRA_DQ22
- U2 pad B5: (no net) -> DDRA_DQ23
- U2 pad B8: (no net) -> DDRA_DQ24
- U2 pad B9: (no net) -> DDRA_DQ25
- U2 pad C1: (no net) -> DDRA_DQ29
- U2 pad C10: (no net) -> DDRA_DQS_C0
- U2 pad C11: (no net) -> DDRA_DQS_C1
- U2 pad C12: (no net) -> DDRA_DQS_C2
- U2 pad C2: (no net) -> DDRA_DQ30
- U2 pad C3: (no net) -> DDRA_DQ31
- U2 pad C4: (no net) -> DDRA_DQS_T0
- U2 pad C5: (no net) -> DDRA_DQS_T1
- U2 pad C8: (no net) -> DDRA_DQS_T2
- U2 pad C9: (no net) -> DDRA_DQS_T3
- U2 pad D1: (no net) -> DDRA_DQS_C3
- U2 pad D10: (no net) -> +1V1_DDR
- U2 pad D11: (no net) -> +1V1_DDR
- U2 pad D12: (no net) -> +1V1_DDR
- U2 pad D2: (no net) -> DDRA_DMI0
- U2 pad D3: (no net) -> DDRA_DMI1
- U2 pad D4: (no net) -> DDRA_DMI2
- U2 pad D5: (no net) -> DDRA_DMI3
- U2 pad D8: (no net) -> +1V8
- U2 pad D9: (no net) -> +1V8
- U2 pad E1: (no net) -> +1V1_DDR
- U2 pad E2: (no net) -> GND
- U2 pad E3: (no net) -> GND
- U2 pad E4: (no net) -> GND
- U20 pad 1: (no net) -> +12V
- U20 pad 2: (no net) -> +12V
- U20 pad 20: (no net) -> SW_VCCINT
- U20 pad 21: (no net) -> SW_VCCINT
- U20 pad 22: (no net) -> SW_VCCINT
- U20 pad 23: (no net) -> POR_B
- U20 pad 24: (no net) -> GND
- U20 pad 3: (no net) -> +12V
- U20 pad 30: (no net) -> GND
- U20 pad 4: (no net) -> EN_VERSAL
- U20 pad 41: (no net) -> GND
- U20 pad 5: (no net) -> I2C3_SCL
- U20 pad 6: (no net) -> I2C3_SDA
- U20 pad 7: (no net) -> VCCINT_0V8
- U20 pad 8: (no net) -> GND
- U21 pad 1: (no net) -> +12V
- U21 pad 2: (no net) -> +12V
- U21 pad 20: (no net) -> SW_AIE
- U21 pad 21: (no net) -> SW_AIE
- U21 pad 22: (no net) -> SW_AIE
- U21 pad 23: (no net) -> POR_B
- U21 pad 24: (no net) -> GND
- U21 pad 3: (no net) -> +12V
- U21 pad 30: (no net) -> GND
- U21 pad 4: (no net) -> EN_VERSAL
- U21 pad 41: (no net) -> GND
- U21 pad 5: (no net) -> I2C3_SCL
- U21 pad 6: (no net) -> I2C3_SDA
- U21 pad 7: (no net) -> VCC_AIE_0V8
- U21 pad 8: (no net) -> GND
- U22 pad 1: (no net) -> +12V
- U22 pad 10: (no net) -> SW_3V3
- U22 pad 11: (no net) -> SW_3V3
- U22 pad 12: (no net) -> unconnected-(U22-PG-Pad12)
- U22 pad 13: (no net) -> BST_3V3
- U22 pad 14: (no net) -> INTVCC_3V3
- U22 pad 17: (no net) -> GND
- U22 pad 2: (no net) -> +12V
- U22 pad 25: (no net) -> GND
- U22 pad 3: (no net) -> EN_VERSAL
- U22 pad 4: (no net) -> FB_3V3
- U22 pad 5: (no net) -> RT_3V3
- U3 pad A1: (no net) -> DDRB_CA0
- U3 pad A10: (no net) -> DDRB_CKE
- U3 pad A11: (no net) -> DDRB_CK_T
- U3 pad A12: (no net) -> DDRB_CK_C
- U3 pad A2: (no net) -> DDRB_CA1
- U3 pad A3: (no net) -> DDRB_CA2
- U3 pad A4: (no net) -> DDRB_CA3
- U3 pad A5: (no net) -> DDRB_CA4
- U3 pad A8: (no net) -> DDRB_CA5
- U3 pad A9: (no net) -> DDRB_CS
- U3 pad AA1: (no net) -> DDRB_RESET_N
- U3 pad AA10: (no net) -> DDRB_DQ6
- U3 pad AA11: (no net) -> DDRB_DQ7
- U3 pad AA12: (no net) -> DDRB_DQ8
- U3 pad AA2: (no net) -> DDRB_DQ0
- U3 pad AA3: (no net) -> DDRB_DQ1
- U3 pad AA4: (no net) -> DDRB_DQ2
- U3 pad AA5: (no net) -> DDRB_DQ3
- U3 pad AA8: (no net) -> DDRB_DQ4
- U3 pad AA9: (no net) -> DDRB_DQ5
- U3 pad AB1: (no net) -> DDRB_DQ9
- U3 pad AB10: (no net) -> DDRB_DQ16
- U3 pad AB11: (no net) -> DDRB_DQ17
- U3 pad AB12: (no net) -> DDRB_DQ18
- U3 pad AB2: (no net) -> DDRB_DQ10
- U3 pad AB3: (no net) -> DDRB_DQ11
- U3 pad AB4: (no net) -> DDRB_DQ12
- U3 pad AB5: (no net) -> DDRB_DQ13
- U3 pad AB8: (no net) -> DDRB_DQ14
- U3 pad AB9: (no net) -> DDRB_DQ15
- U3 pad B1: (no net) -> DDRB_DQ19
- U3 pad B10: (no net) -> DDRB_DQ26
- U3 pad B11: (no net) -> DDRB_DQ27
- U3 pad B12: (no net) -> DDRB_DQ28
- U3 pad B2: (no net) -> DDRB_DQ20
- U3 pad B3: (no net) -> DDRB_DQ21
- U3 pad B4: (no net) -> DDRB_DQ22
- U3 pad B5: (no net) -> DDRB_DQ23
- U3 pad B8: (no net) -> DDRB_DQ24
- U3 pad B9: (no net) -> DDRB_DQ25
- U3 pad C1: (no net) -> DDRB_DQ29
- U3 pad C10: (no net) -> DDRB_DQS_C0
- U3 pad C11: (no net) -> DDRB_DQS_C1
- U3 pad C12: (no net) -> DDRB_DQS_C2
- U3 pad C2: (no net) -> DDRB_DQ30
- U3 pad C3: (no net) -> DDRB_DQ31
- U3 pad C4: (no net) -> DDRB_DQS_T0
- U3 pad C5: (no net) -> DDRB_DQS_T1
- U3 pad C8: (no net) -> DDRB_DQS_T2
- U3 pad C9: (no net) -> DDRB_DQS_T3
- U3 pad D1: (no net) -> DDRB_DQS_C3
- U3 pad D10: (no net) -> +1V1_DDR
- U3 pad D11: (no net) -> +1V1_DDR
- U3 pad D12: (no net) -> +1V1_DDR
- U3 pad D2: (no net) -> DDRB_DMI0
- U3 pad D3: (no net) -> DDRB_DMI1
- U3 pad D4: (no net) -> DDRB_DMI2
- U3 pad D5: (no net) -> DDRB_DMI3
- U3 pad D8: (no net) -> +1V8
- U3 pad D9: (no net) -> +1V8
- U3 pad E1: (no net) -> +1V1_DDR
- U3 pad E2: (no net) -> GND
- U3 pad E3: (no net) -> GND
- U3 pad E4: (no net) -> GND
- U4 pad A1: (no net) -> EMMC_CLK
- U4 pad A10: (no net) -> EMMC_D6
- U4 pad A11: (no net) -> EMMC_D7
- U4 pad A12: (no net) -> +3V3
- U4 pad A13: (no net) -> +3V3
- U4 pad A14: (no net) -> +1V8
- U4 pad A2: (no net) -> EMMC_CMD
- U4 pad A3: (no net) -> EMMC_RST_N
- U4 pad A4: (no net) -> EMMC_D0
- U4 pad A5: (no net) -> EMMC_D1
- U4 pad A6: (no net) -> EMMC_D2
- U4 pad A7: (no net) -> EMMC_D3
- U4 pad A8: (no net) -> EMMC_D4
- U4 pad A9: (no net) -> EMMC_D5
- U4 pad B1: (no net) -> +1V8
- U4 pad B2: (no net) -> EMMC_VDDI
- U4 pad B3: (no net) -> GND
- U4 pad B4: (no net) -> GND
- U5 pad 1: (no net) -> QSPI_CS_N
- U5 pad 2: (no net) -> QSPI_DQ1
- U5 pad 3: (no net) -> QSPI_DQ2
- U5 pad 4: (no net) -> GND
- U5 pad 5: (no net) -> QSPI_DQ0
- U5 pad 6: (no net) -> QSPI_CLK
- U5 pad 7: (no net) -> QSPI_DQ3
- U5 pad 8: (no net) -> +1V8
- U5 pad 9: (no net) -> GND
- U6 pad 1: (no net) -> RGMII_TXC
- U6 pad 10: (no net) -> RGMII_RXD1
- U6 pad 11: (no net) -> RGMII_RXD2
- U6 pad 12: (no net) -> RGMII_RXD3
- U6 pad 13: (no net) -> MDC
- U6 pad 14: (no net) -> MDIO
- U6 pad 15: (no net) -> PHY_RST_N
- U6 pad 16: (no net) -> PHY_INT_N
- U6 pad 17: (no net) -> PHY_MD1
- U6 pad 18: (no net) -> PHY_MD2
- U6 pad 19: (no net) -> PHY_MD3
- U6 pad 2: (no net) -> RGMII_TX_CTL
- U6 pad 20: (no net) -> PHY_MD4
- U6 pad 21: (no net) -> PHY_MD5
- U6 pad 22: (no net) -> PHY_MD6
- U6 pad 23: (no net) -> PHY_MD7
- U6 pad 24: (no net) -> PHY_MD8
- U6 pad 26: (no net) -> PHY_XI
- U6 pad 3: (no net) -> RGMII_TXD0
- U6 pad 30: (no net) -> +2V5
- U6 pad 31: (no net) -> +2V5
- U6 pad 32: (no net) -> +1V0_PHY
- U6 pad 33: (no net) -> +1V0_PHY
- U6 pad 34: (no net) -> +1V8
- U6 pad 35: (no net) -> +1V8
- U6 pad 36: (no net) -> GND
- U6 pad 4: (no net) -> RGMII_TXD1
- U6 pad 49: (no net) -> GND
- U6 pad 5: (no net) -> RGMII_TXD2
- U6 pad 6: (no net) -> RGMII_TXD3
- U6 pad 7: (no net) -> RGMII_RXC
- U6 pad 8: (no net) -> RGMII_RX_CTL
- U6 pad 9: (no net) -> RGMII_RXD0
- U7 pad 1: (no net) -> +3V3
- U7 pad 10: (no net) -> ID_PA2
- U7 pad 11: (no net) -> ID_PA3
- U7 pad 12: (no net) -> VIN_SENSE
- U7 pad 13: (no net) -> V28_SENSE
- U7 pad 14: (no net) -> V5_SENSE
- U7 pad 15: (no net) -> GND
- U7 pad 16: (no net) -> +3V3
- U7 pad 17: (no net) -> V3V3_SENSE
- U7 pad 18: (no net) -> CS_BF0
- U7 pad 19: (no net) -> MCU_SPI_SCK
- U7 pad 2: (no net) -> unconnected-(U7-PC13-Pad2)
- U7 pad 20: (no net) -> MCU_SPI_MISO
- U7 pad 21: (no net) -> MCU_SPI_MOSI
- U7 pad 22: (no net) -> unconnected-(U7-PC4-Pad22)
- U7 pad 23: (no net) -> unconnected-(U7-PC5-Pad23)
- U7 pad 24: (no net) -> NTC_RFIC
- U7 pad 25: (no net) -> VNEG_SENSE
- U7 pad 26: (no net) -> unconnected-(U7-PB2-Pad26)
- U7 pad 27: (no net) -> GND
- U7 pad 28: (no net) -> +3V3
- U7 pad 29: (no net) -> +3V3
- U7 pad 3: (no net) -> unconnected-(U7-PC14-Pad3)
- U7 pad 30: (no net) -> unconnected-(U7-PB10-Pad30)
- U7 pad 31: (no net) -> GND
- U7 pad 32: (no net) -> +3V3
- U7 pad 33: (no net) -> NTC_HOUSING
- U7 pad 34: (no net) -> ID_PA6
- U7 pad 35: (no net) -> unconnected-(U7-PB13-Pad35)
- U7 pad 36: (no net) -> ID_PA4
- U7 pad 37: (no net) -> unconnected-(U7-PB15-Pad37)
- U7 pad 38: (no net) -> EN_VERSAL
- U7 pad 39: (no net) -> EN_HEATER
- U7 pad 4: (no net) -> unconnected-(U7-PC15-Pad4)
- U7 pad 40: (no net) -> I2C3_SCL
- U7 pad 41: (no net) -> I2C3_SDA
- U7 pad 42: (no net) -> EN_DRAIN_SW
- U7 pad 43: (no net) -> UART_M2V
- U7 pad 44: (no net) -> UART_V2M
- U7 pad 45: (no net) -> unconnected-(U7-PA11-Pad45)
- U7 pad 46: (no net) -> unconnected-(U7-PA12-Pad46)
- U7 pad 47: (no net) -> GND
- U7 pad 48: (no net) -> +3V3
- U7 pad 49: (no net) -> SWDIO
- U7 pad 5: (no net) -> ID_PA5
- U7 pad 50: (no net) -> SWCLK
- U7 pad 51: (no net) -> CS_BF1
- U7 pad 52: (no net) -> PLL_LD_TX
- U7 pad 53: (no net) -> PLL_LD_LO
- U7 pad 54: (no net) -> NEG_PGOOD
- U7 pad 55: (no net) -> unconnected-(U7-PD2-Pad55)
- U7 pad 56: (no net) -> unconnected-(U7-PB3-Pad56)
- U7 pad 57: (no net) -> EN_NEG5
- U7 pad 58: (no net) -> EN_28V
- U7 pad 59: (no net) -> TX_MUTE_N
- U7 pad 6: (no net) -> unconnected-(U7-PF1-Pad6)
- U7 pad 60: (no net) -> EN_RF_5V
- U7 pad 61: (no net) -> unconnected-(U7-PB8-Pad61)
- U7 pad 62: (no net) -> unconnected-(U7-PB9-Pad62)
- U7 pad 63: (no net) -> GND
- U7 pad 64: (no net) -> +3V3
- U7 pad 7: (no net) -> NRST
- U7 pad 8: (no net) -> VNEG_SENSE
- U7 pad 9: (no net) -> ID_PA1
- U8 pad 1: (no net) -> unconnected-(U8-~{SAFEBOOT}-Pad1)
- U8 pad 10: (no net) -> GND
- U8 pad 11: (no net) -> GNSS_RF
- U8 pad 12: (no net) -> GND
- U8 pad 13: (no net) -> GND
- U8 pad 14: (no net) -> unconnected-(U8-LNA_EN-Pad14)
- U8 pad 15: (no net) -> unconnected-(U8-RESERVED-Pad15)
- U8 pad 16: (no net) -> unconnected-(U8-RESERVED-Pad16)
- U8 pad 17: (no net) -> unconnected-(U8-RESERVED-Pad17)
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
